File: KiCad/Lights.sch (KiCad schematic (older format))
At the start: 12 parts

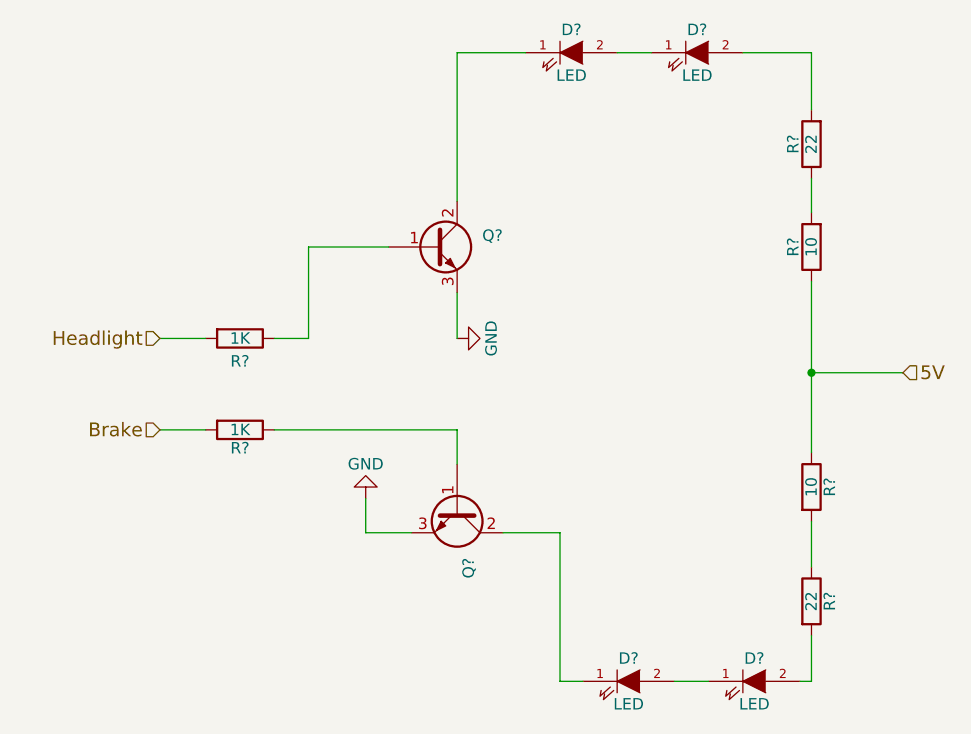
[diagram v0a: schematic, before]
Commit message: Updated the schematics and started with the PCB
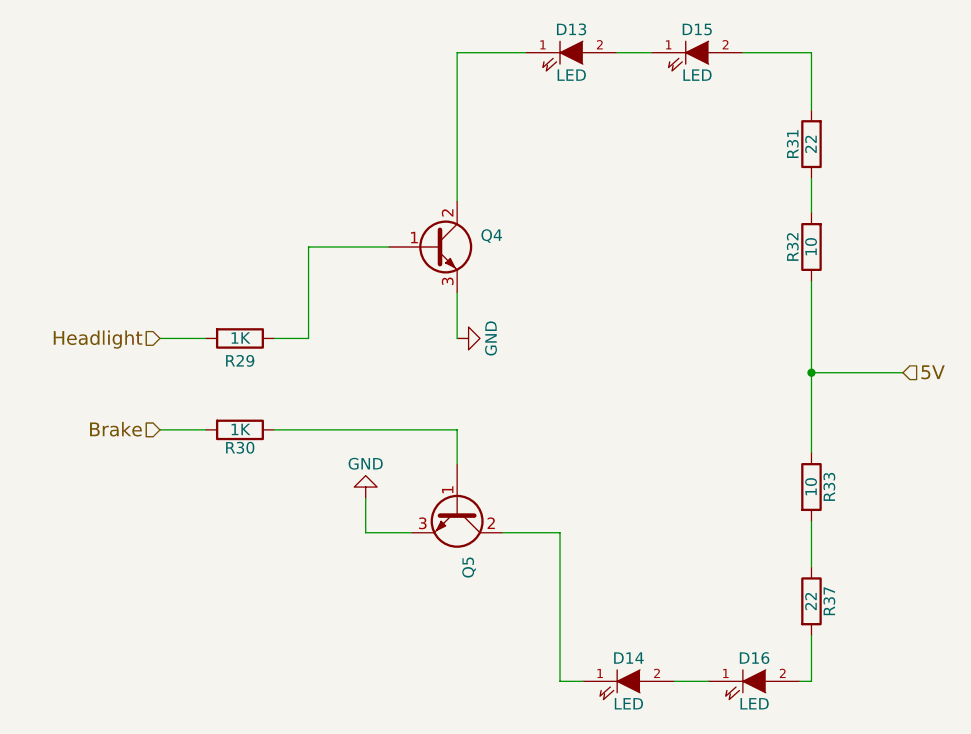
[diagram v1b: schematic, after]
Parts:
- D13, D14, D15, D16: renamed from D?; footprint (none) -> Wire_Connections_Bridges:WireConnection_1.50mmDrill
- Q4, Q5: renamed from Q?; footprint (none) -> TO_SOT_Packages_THT:TO-92_Inline_Narrow_Oval
- R29, R30, R31, R32, R33, R37: renamed from R?; footprint (none) -> Resistors_ThroughHole:Resistor_Vertical_RM5mm
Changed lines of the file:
@@
 $Descr A4 11693 8268
 encoding utf-8
-Sheet 5 7
+Sheet 5 6
 Title ""
 Date ""
@@
 $EndDescr
 $Comp
-L LED D?
+L LED D13
 U 1 1 57167226
 P 5100 1350
-F 0 "D?" H 5100 1450 50  0000 C CNN
+F 0 "D13" H 5100 1450 50  0000 C CNN
 F 1 "LED" H 5100 1250 50  0000 C CNN
-F 2 "" H 5100 1350 50  0000 C CNN
+F 2 "Wire_Connections_Bridges:WireConnection_1.50mmDrill" H 5100 1350 50  0001 C CNN
 F 3 "" H 5100 1350 50  0000 C CNN
 	1    5100 1350
@@
 $EndComp
 $Comp
-L LED D?
+L LED D15
 U 1 1 571672D8
 P 5650 1350
-F 0 "D?" H 5650 1450 50  0000 C CNN
+F 0 "D15" H 5650 1450 50  0000 C CNN
 F 1 "LED" H 5650 1250 50  0000 C CNN
-F 2 "" H 5650 1350 50  0000 C CNN
+F 2 "Wire_Connections_Bridges:WireConnection_1.50mmDrill" H 5650 1350 50  0001 C CNN
 F 3 "" H 5650 1350 50  0000 C CNN
 	1    5650 1350
@@
 $EndComp
 $Comp
-L LED D?
+L LED D14
 U 1 1 571673C6
 P 5350 4100
-F 0 "D?" H 5350 4200 50  0000 C CNN
+F 0 "D14" H 5350 4200 50  0000 C CNN
 F 1 "LED" H 5350 4000 50  0000 C CNN
-F 2 "" H 5350 4100 50  0000 C CNN
+F 2 "Wire_Connections_Bridges:WireConnection_1.50mmDrill" H 5350 4100 50  0001 C CNN
 F 3 "" H 5350 4100 50  0000 C CNN
 	1    5350 4100
@@
 $EndComp
 $Comp
-L LED D?
+L LED D16
 U 1 1 5716743B
 P 5900 4100
-F 0 "D?" H 5900 4200 50  0000 C CNN
+F 0 "D16" H 5900 4200 50  0000 C CNN
 F 1 "LED" H 5900 4000 50  0000 C CNN
-F 2 "" H 5900 4100 50  0000 C CNN
+F 2 "Wire_Connections_Bridges:WireConnection_1.50mmDrill" H 5900 4100 50  0001 C CNN
 F 3 "" H 5900 4100 50  0000 C CNN
 	1    5900 4100
@@
 $EndComp
 $Comp
-L Q_NPN_BCE Q?
+L Q_NPN_BCE Q4
 U 1 1 571675BE
 P 4500 2200
-F 0 "Q?" H 4800 2250 50  0000 R CNN
+F 0 "Q4" H 4800 2250 50  0000 R CNN
 F 1 "Q_NPN_BCE" H 5100 2150 50  0001 R CNN
-F 2 "" H 4700 2300 50  0000 C CNN
+F 2 "TO_SOT_Packages_THT:TO-92_Inline_Narrow_Oval" H 4700 2300 50  0001 C CNN
 F 3 "" H 4500 2200 50  0000 C CNN
 	1    4500 2200
@@
 $EndComp
 $Comp
-L Q_NPN_BCE Q?
+L Q_NPN_BCE Q5
 U 1 1 57167694
 P 4600 3350
-F 0 "Q?" H 4900 3400 50  0000 R CNN
+F 0 "Q5" H 4900 3400 50  0000 R CNN
 F 1 "NPN" H 5200 3300 50  0001 L TNN
-F 2 "" H 4800 3450 50  0000 C CNN
+F 2 "TO_SOT_Packages_THT:TO-92_Inline_Narrow_Oval" H 4800 3450 50  0001 C CNN
 F 3 "" H 4600 3350 50  0000 C CNN
 	1    4600 3350
@@
 Headlight
 $Comp
-L R R?
+L R R29
 U 1 1 5716799C
 P 3650 2600
-F 0 "R?" V 3750 2600 50  0000 C CNN
+F 0 "R29" V 3750 2600 50  0000 C CNN
 F 1 "1K" V 3650 2600 50  0000 C CNN
-F 2 "" V 3580 2600 50  0000 C CNN
+F 2 "Resistors_ThroughHole:Resistor_Vertical_RM5mm" V 3580 2600 50  0001 C CNN
 F 3 "" H 3650 2600 50  0000 C CNN
 	1    3650 2600
@@
 $EndComp
 $Comp
-L R R?
+L R R30
 U 1 1 57167A65
 P 3650 3000
-F 0 "R?" V 3730 3000 50  0000 C CNN
+F 0 "R30" V 3730 3000 50  0000 C CNN
 F 1 "1K" V 3650 3000 50  0000 C CNN
-F 2 "" V 3580 3000 50  0000 C CNN
+F 2 "Resistors_ThroughHole:Resistor_Vertical_RM5mm" V 3580 3000 50  0001 C CNN
 F 3 "" H 3650 3000 50  0000 C CNN
 	1    3650 3000
@@
 $EndComp
 $Comp
-L R R?
+L R R32
 U 1 1 57167B98
 P 6150 2200
-F 0 "R?" V 6230 2200 50  0000 C CNN
+F 0 "R32" V 6230 2200 50  0000 C CNN
 F 1 "10" V 6150 2200 50  0000 C CNN
-F 2 "" V 6080 2200 50  0000 C CNN
+F 2 "Resistors_ThroughHole:Resistor_Vertical_RM5mm" V 6080 2200 50  0001 C CNN
 F 3 "" H 6150 2200 50  0000 C CNN
 	1    6150 2200
@@
 $EndComp
 $Comp
-L GND #PWR?
+L GND #PWR020
 U 1 1 57167CC8
 P 4600 2600
-F 0 "#PWR?" H 4600 2350 50  0001 C CNN
+F 0 "#PWR020" H 4600 2350 50  0001 C CNN
 F 1 "GND" H 4600 2450 50  0000 C CNN
 F 2 "" H 4600 2600 50  0000 C CNN
@@
 $EndComp
 $Comp
-L GND #PWR?
+L GND #PWR021
 U 1 1 57168248
 P 4200 3300
-F 0 "#PWR?" H 4200 3050 50  0001 C CNN
+F 0 "#PWR021" H 4200 3050 50  0001 C CNN
 F 1 "GND" H 4200 3150 50  0000 C CNN
 F 2 "" H 4200 3300 50  0000 C CNN
@@
 $EndComp
 $Comp
-L R R?
+L R R33
 U 1 1 571684E0
 P 6150 3250
-F 0 "R?" V 6230 3250 50  0000 C CNN
+F 0 "R33" V 6230 3250 50  0000 C CNN
 F 1 "10" V 6150 3250 50  0000 C CNN
-F 2 "" V 6080 3250 50  0000 C CNN
+F 2 "Resistors_ThroughHole:Resistor_Vertical_RM5mm" V 6080 3250 50  0001 C CNN
 F 3 "" H 6150 3250 50  0000 C CNN
 	1    6150 3250
@@
 Connection ~ 6150 2750
 $Comp
-L R R?
+L R R31
 U 1 1 571B4C7D
 P 6150 1750
-F 0 "R?" V 6230 1750 50  0000 C CNN
+F 0 "R31" V 6230 1750 50  0000 C CNN
 F 1 "22" V 6150 1750 50  0000 C CNN
-F 2 "" V 6080 1750 50  0000 C CNN
+F 2 "Resistors_ThroughHole:Resistor_Vertical_RM5mm" V 6080 1750 50  0001 C CNN
 F 3 "" H 6150 1750 50  0000 C CNN
 	1    6150 1750
@@
 	5850 1350 6150 1350
 $Comp
-L R R?
+L R R37
 U 1 1 571B5113
 P 6150 3750
-F 0 "R?" V 6230 3750 50  0000 C CNN
+F 0 "R37" V 6230 3750 50  0000 C CNN
 F 1 "22" V 6150 3750 50  0000 C CNN
-F 2 "" V 6080 3750 50  0000 C CNN
+F 2 "Resistors_ThroughHole:Resistor_Vertical_RM5mm" V 6080 3750 50  0001 C CNN
 F 3 "" H 6150 3750 50  0000 C CNN
 	1    6150 3750
